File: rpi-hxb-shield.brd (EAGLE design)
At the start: 33.5 x 35 mm, 24 parts, among them Q1 CRYSTALX22, U2 24LC128-I/SN

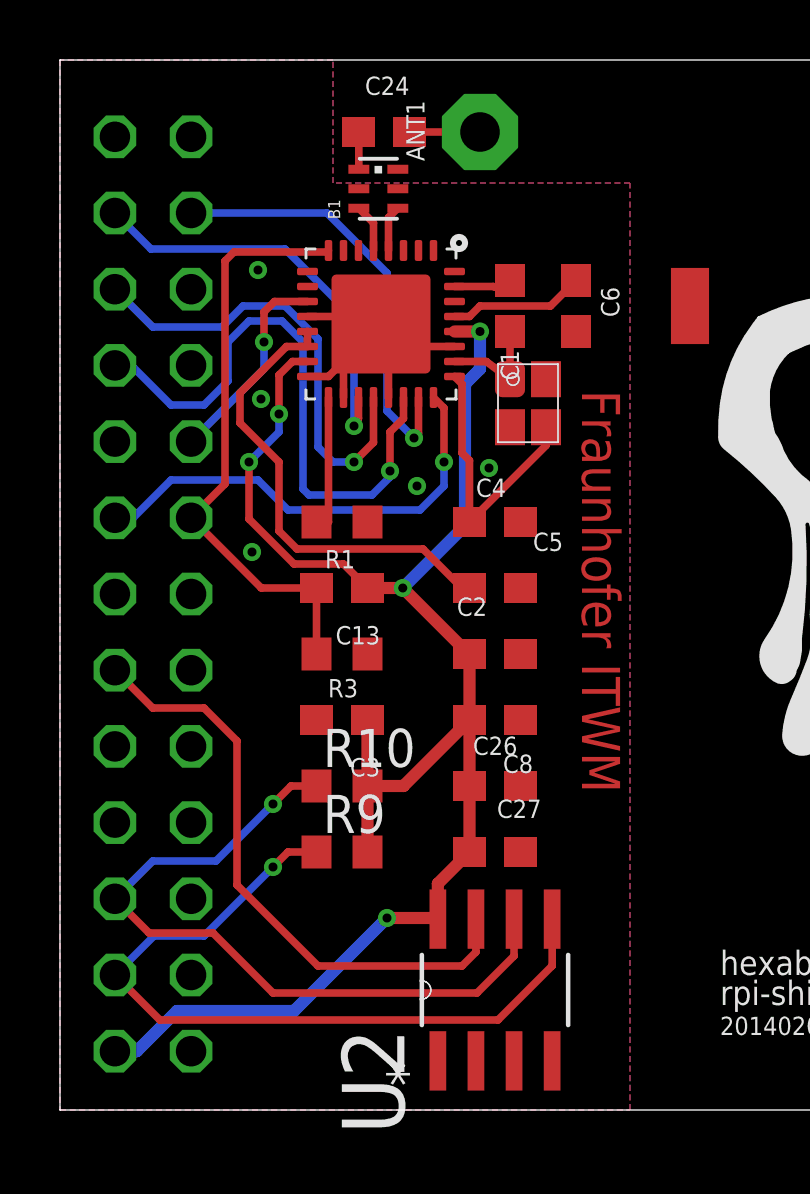
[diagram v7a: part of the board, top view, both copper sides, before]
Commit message: removed CLKM and according resistir
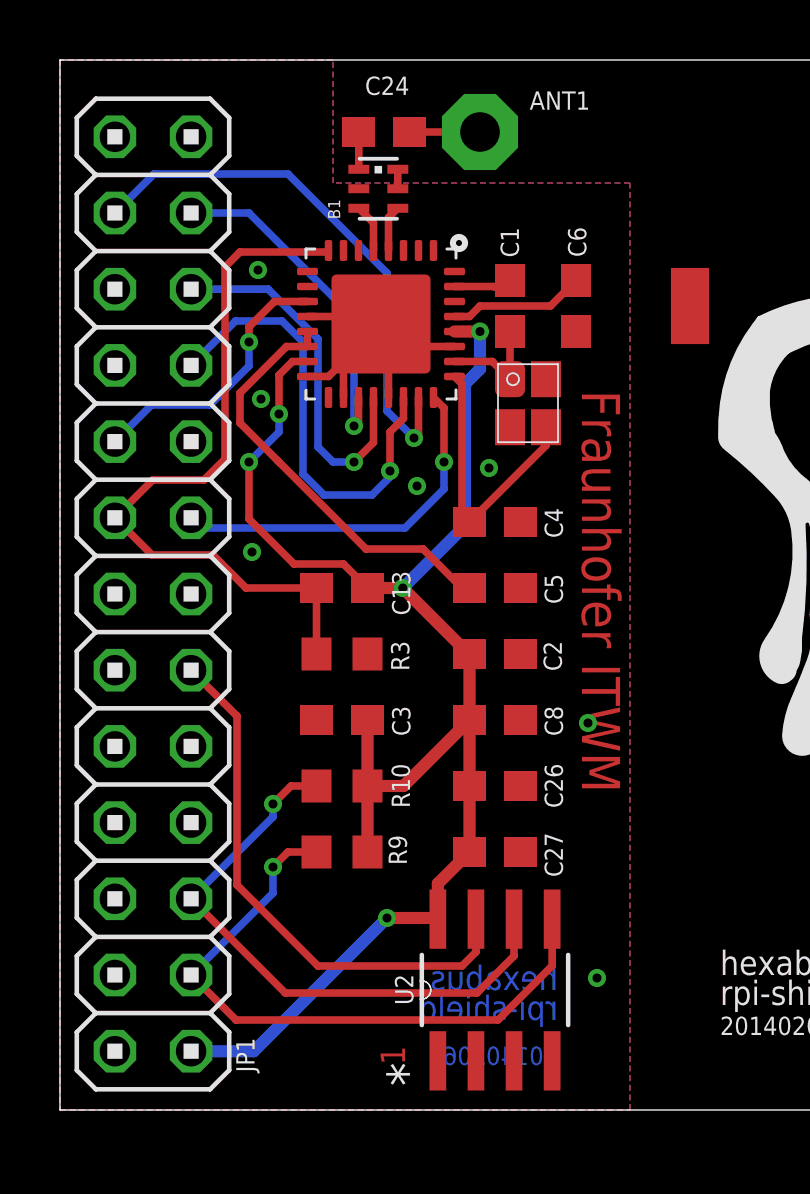
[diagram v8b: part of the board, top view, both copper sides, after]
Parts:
- removed R1: 470R, rcl:R0603
- flipped JP1 to the top
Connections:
- removed net CLKM: R1.1
- removed net N$5: R1.2, U1.17
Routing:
- net SCL: track 24.6 -> 19.8 mm
- net MOSI: track 20.0 -> 15.3 mm
- net SDA: track 25.9 -> 21.3 mm
- net N$5: track 4.55 -> 0.00 mm
- net AT_RST: track 20.0 -> 24.4 mm
- net SEL1: track 14.6 -> 18.3 mm
- net MISO: track 15.5 -> 12.3 mm
- net IRQ: track 15.3 -> 12.3 mm
- net VCC: track 57.0 -> 54.4 mm
- net SCLK: track 14.0 -> 11.5 mm
- net SLP_TR: track 6.92 -> 9.12 mm
- net WP: track 20.2 -> 18.2 mm
- net N$2: track 15.7 -> 14.3 mm
- net GND: track 13.6 -> 14.3 mm, vias 5 -> 7
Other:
- board text added: "1"
